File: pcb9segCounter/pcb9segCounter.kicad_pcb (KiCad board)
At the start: 2 copper layers, 72.2 x 78.5 mm, 57 parts, among them J1 AVR-ISP-6, J2 SAO, U1 ATtiny84A-SS

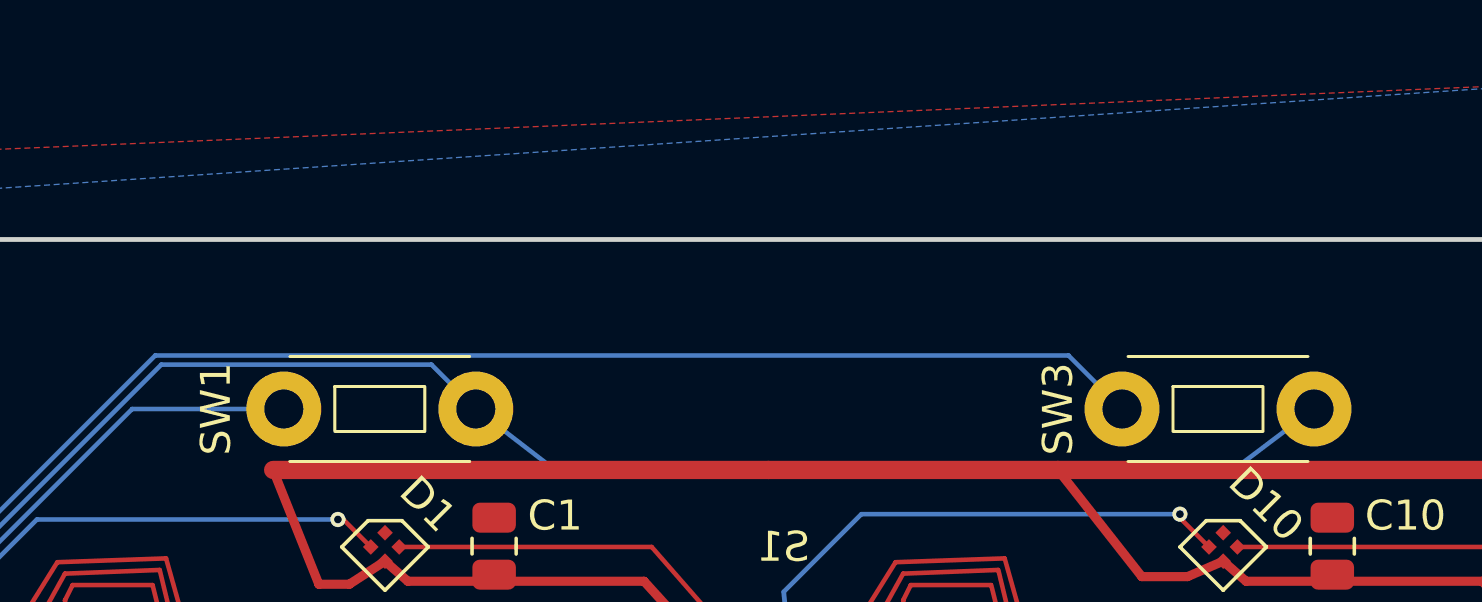
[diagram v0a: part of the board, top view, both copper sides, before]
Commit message: Added website to board, generated gerber which was sent to oshpark for manufacture
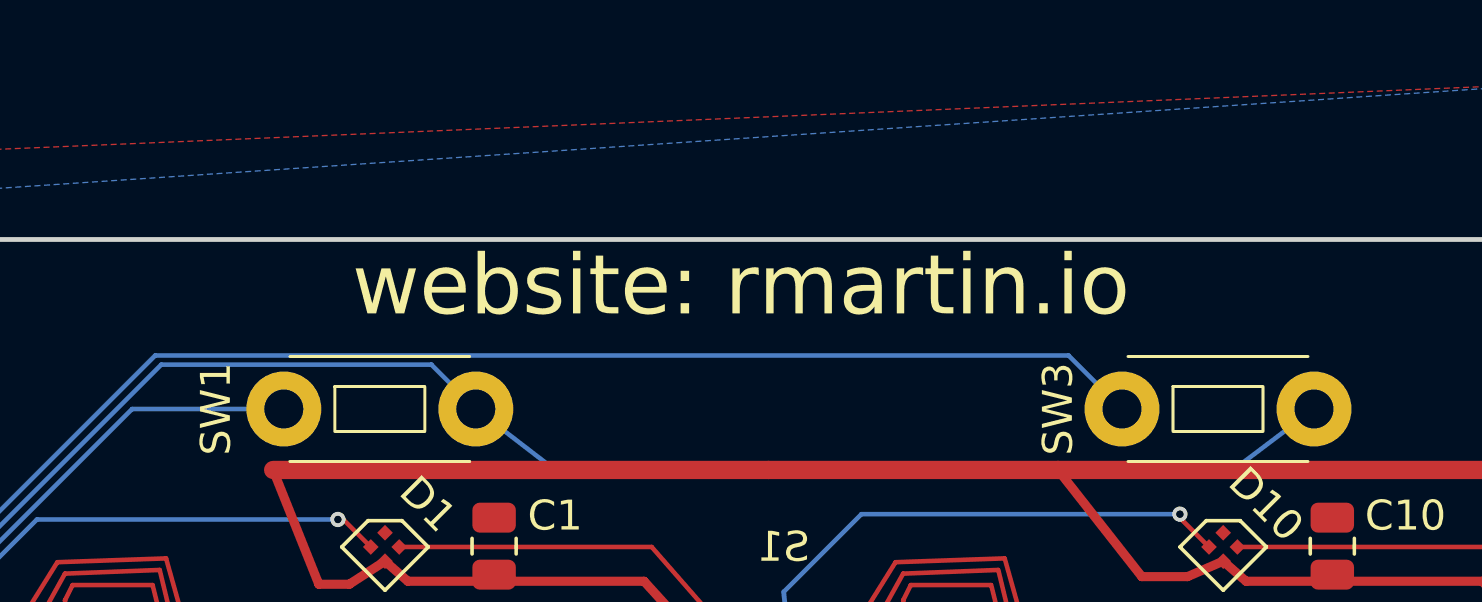
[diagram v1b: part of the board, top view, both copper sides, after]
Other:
- board text added: "website: rmartin.io"
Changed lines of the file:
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@@
 			(outputformat 1)
 			(mirror no)
-			(drillshape 1)
+			(drillshape 0)
 			(scaleselection 1)
-			(outputdirectory "")
+			(outputdirectory "gerber9SegCounter/")
 		)
 	)
@@
 		)
 	)
+	(gr_text "website: rmartin.io"
+		(at 87.4776 39.4208 0)
+		(layer "F.SilkS")
+		(effects
+			(font
+				(size 2 2)
+				(thickness 0.3)
+			)
+			(justify top)
+		)
+	)

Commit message: Made edits to PCB file and generated gerbers for manufacture at JLCPCB
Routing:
- net +5V: track 491.8 -> 492.7 mm
